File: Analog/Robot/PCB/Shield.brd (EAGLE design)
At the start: 160 x 100 mm, 5 parts, among them IC2 LM2574HVN-3.3

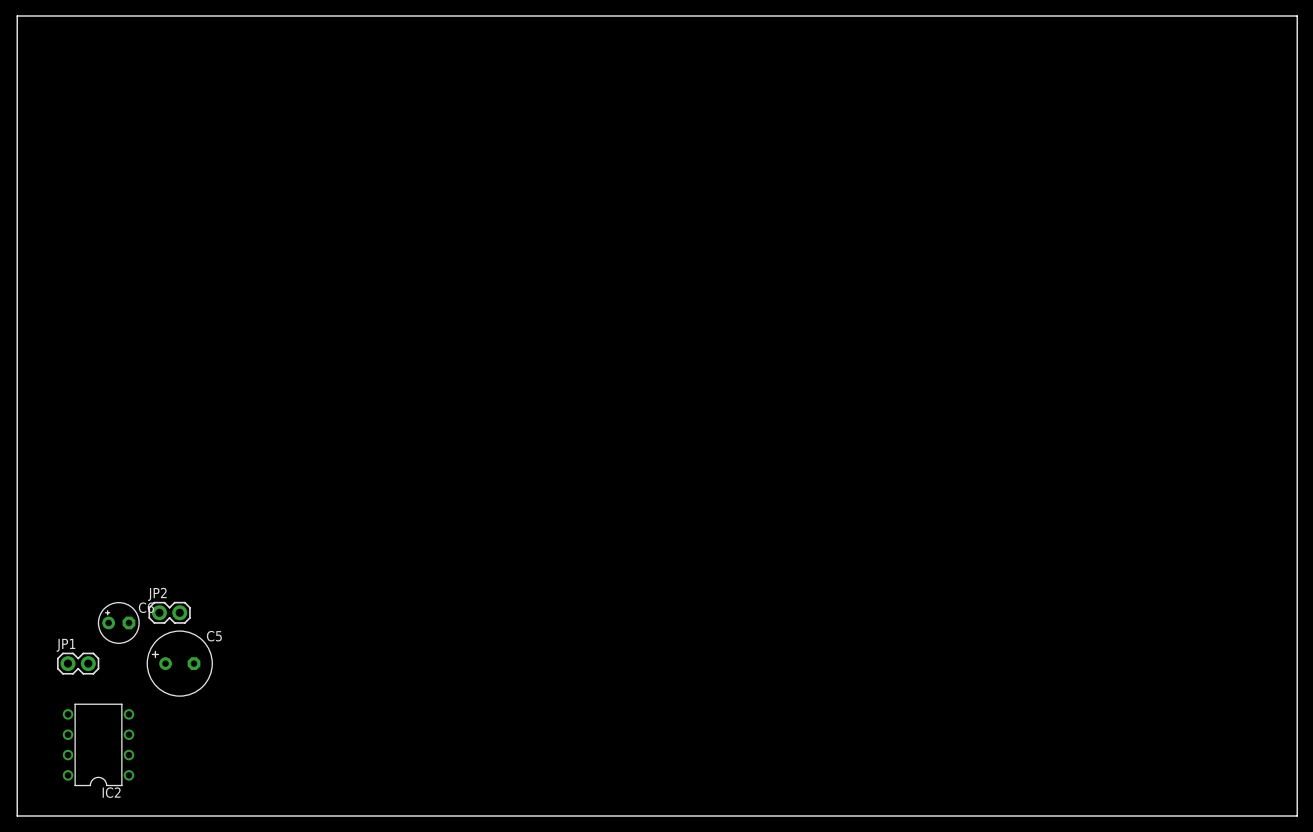
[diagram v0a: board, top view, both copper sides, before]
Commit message: PCB and firmware
Gate PCB 70% completed, need to figure out pinout for MCU and layout
signal amps.  Board size reduced by 50%.  Also need to add testpoints
Robot PCB PSU layout completed, motor and stepper drivers will move to
separate PCB
Created firmware files, w/o code
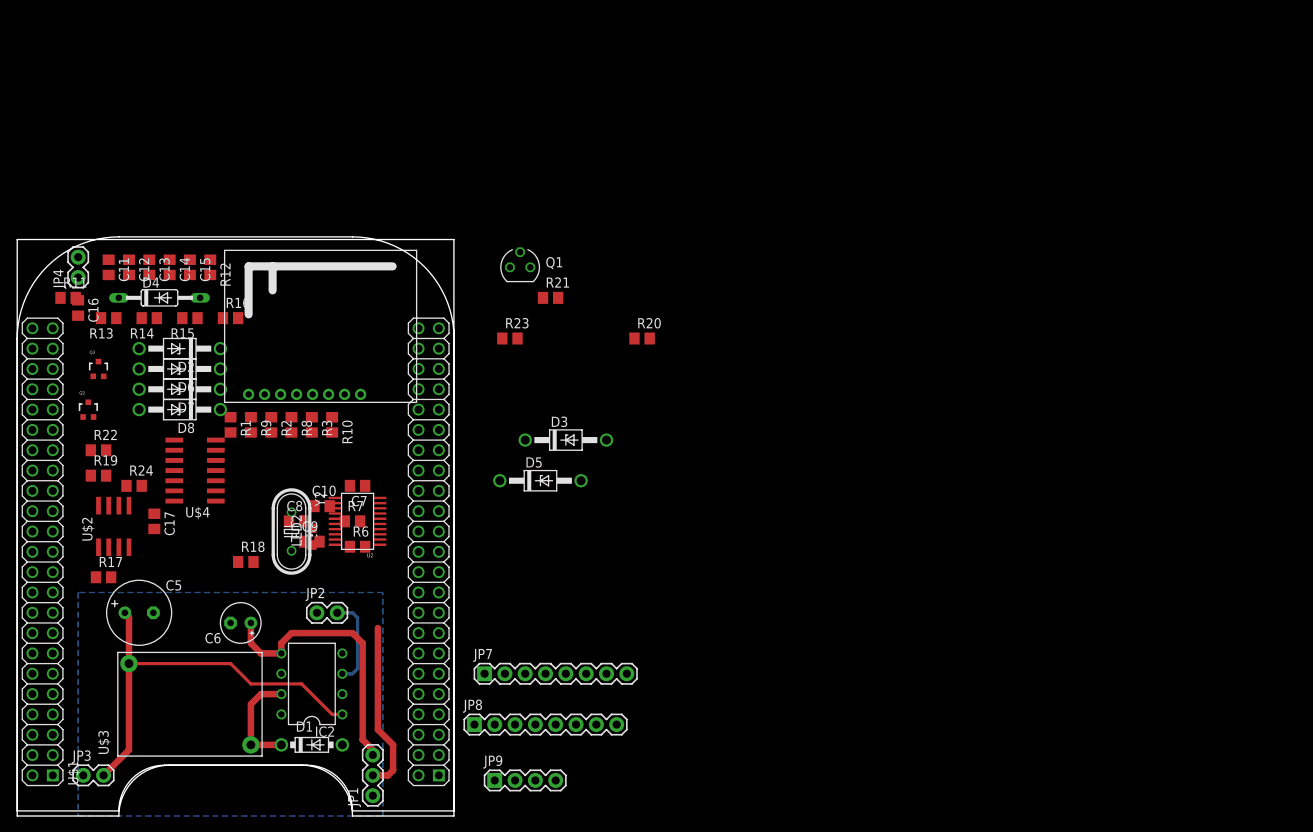
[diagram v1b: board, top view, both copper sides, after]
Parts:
- added C10: 1nF, rcl:C0805
- added C11, C12, C13, C14, C15, C16: (no value), rcl:C0805
- added C17: 10nF, rcl:C0805
- added C7: 0.1uF, rcl:C0805
- added C8, C9: 12pF, rcl:C0805
- added D1: 1N5819-B, diode:DO41-7.6
- added D2, D3, D7, D8: 1N4742A, diode:DO41Z10
- added D4: 1N4148DO35-10, diode:DO35-10
- added D5, D6: 1N4728, diode:DO41Z10
- added JP3, JP4: M02PTH, SparkFun-Connectors:1X02
- added JP7, JP8: (no value), SparkFun-Connectors:1X08
- added JP9: (no value), SparkFun-Connectors:1X04
- added LED2: (no value), led:CHIP-LED0805
- added Q1: BS250, transistor-small-signal:SOT54E
- added Q2, Q3: MOSFET-NCHANNEL2N7002PW, SparkFun-DiscreteSemi:SOT323
- added R1, R10, R12, R17, R18, R19, R2, R20, R21, R22, R23, R24, R3, R8, R9: 0, rcl:R0805
- added R11: 5k, rcl:R0805
- added R13, R14, R15, R16: 100k, rcl:R0805
- added R6: 47k, rcl:R0805
- added R7: 470, rcl:R0805
- added U$1: BEAGLEBONE_OUTLINE, adafruit:BEAGLEBONE_SHIELD
- added U$2: LM6482, npol:SOIC8
- added U$3: PE-526XXNL, npol:PE_VERTICAL
- added U$4: MAX4518, npol:SO-14
- added U2: MSP430G2X53_20P, npol:TSSOP20_PW
- added U3: QFM-TRX-24G, npol:QFM-TRX1-24G
- added Y2: (no value), SparkFun-FreqCtrl:HC49U-V
- JP1: value M02PTH -> (none); device SparkFun-Connectors:1X02 -> SparkFun-Connectors:1X03
- moved JP1 41.5 mm to (44.5, 2.54), turned to 90 degrees
- moved IC2 27.7 mm to (36.8, 16.5)
- moved JP2 19.7 mm to (37.5, 25.4)
- moved C6 15.2 mm to (27.9, 24.1), turned to 180 degrees
- moved C5 8.13 mm to (15.2, 25.4)
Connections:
- new net +12V: C17.1, C6.+, IC2.5, JP1.3, R21.2, R22.2, U$2.8, U$4.12
- new net AIN0: U$1.85
- new net DIR: JP7.1
- new net DLED: LED2.C, U2.2
- new net GNDA: C5.-, C6.-, D1.A, IC2.2, IC2.4, JP1.1, JP2.1, JP3.1
- new net MISO: U2.14
- new net MOSI: U2.15
- new net MUX_A0: U$4.1
- new net MUX_A1: U$4.14
- new net MUX_EN: U$4.2
- new net N$10: D4.A, Q1.G, R12.2
- new net N$11: C16.1, D2.C, D4.C, Q2.3, R13.2, U$4.4
- new net N$12: R20.1, R23.2, U$2.6
- new net N$13: R23.1, R24.2, U$2.7
- new net N$14: R18.2, U$4.6
- new net N$15: R17.2, R18.1, U$2.2
- new net N$16: R17.1, R19.2, U$2.1
- new net N$17: JP7.3, JP7.4
- new net N$18: D3.C, R13.1, R14.2, U$4.5
- new net N$19: D7.C, R14.1, R15.2, U$4.11
- new net N$2: LED2.A, R7.1
- new net N$20: D8.C, R15.1, R16.2, U$4.10
- new net N$21: Q1.S, R20.2, R21.1
- new net N$22: Q2.1, Q3.3, R22.1
- new net N$26: JP8.3, JP9.1
- new net N$27: JP8.4, JP9.2
- new net N$28: JP8.5, JP9.3
- new net N$29: JP8.6, JP9.4
- new net N$3: D1.C, IC2.7, U$3.2
- new net N$4: C5.+, IC2.1, JP3.2, U$3.1
- new net N$7: R2.1, R9.1, U3.3
- new net N$8: R1.1, R8.1, U3.2
- new net N$9: C11.1, C12.1, C13.1, C14.1, C15.1, JP4.2, R11.2, R12.1
- new net RFID_RX1: D6.C, R19.1, U2.9
- new net RFID_RX2: D5.C, R24.1, U2.10
- new net RFID_TX: Q3.1, U2.8
- new net RF_MISO: R10.2
- new net RF_MOSI: R8.2
- new net RF_SCK: R9.2
- new net RXD: U2.3
- new net SBWTCK: U2.17
- new net SBWTDIO: C10.1, R6.1, U2.16
- new net SCK: U2.7
- new net SPI0_CS: U$1.63
- new net SPI0_DI: R3.2, U$1.64
- new net SPI0_DO: R1.2, U$1.67
- new net SPI0_SCK: R2.2, U$1.68
- new net STEP: JP7.2
- new net SYS_5V: U$1.53
- new net TXD: U2.4
- new net V+: JP1.2, JP8.8
- new net VDD_5V: U$1.51, U$1.52
- new net XIN: C9.1, U2.19, Y2.2
- new net XOUT: C8.1, U2.18, Y2.1
- net +3V3: now also C7.1, JP8.2, R6.2, R7.2, U$1.49, U$1.50, U2.1, U3.1; no longer C5.+, IC2.1
- net GND: now also C10.2, C11.2, C12.2, C13.2, C14.2, C15.2, C16.2, C17.2, C7.2, C8.2, C9.2, D2.A, D3.A, D5.A, D6.A, D7.A, D8.A, JP4.1, JP8.1, JP8.7, Q1.D, Q2.2, Q3.2, R16.1, U$1.1, U$1.2, U$1.47, U$1.48, U$1.89, U$1.90, U$1.91, U$1.92, U$2.3, U$2.4, U$2.5, U$4.13, U$4.3, U2.20, U3.6; no longer C5.-, C6.-, IC2.2, IC2.4, JP1.1, JP2.1
- net N$5: now also R10.1, R3.1, U3.4; no longer C6.+, IC2.5, JP1.2
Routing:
- net N$4: track 0.00 -> 51.1 mm
- net +12V: track 0.00 -> 33.9 mm
- net V+: track 0.00 -> 21.4 mm
- net N$3: track 0.00 -> 13.2 mm
- net N$6: track 0.00 -> 11.3 mm
- added copper zone on layer 16, net GNDA
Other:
- board size 160 x 100 mm -> 54.6 x 72.1 mm

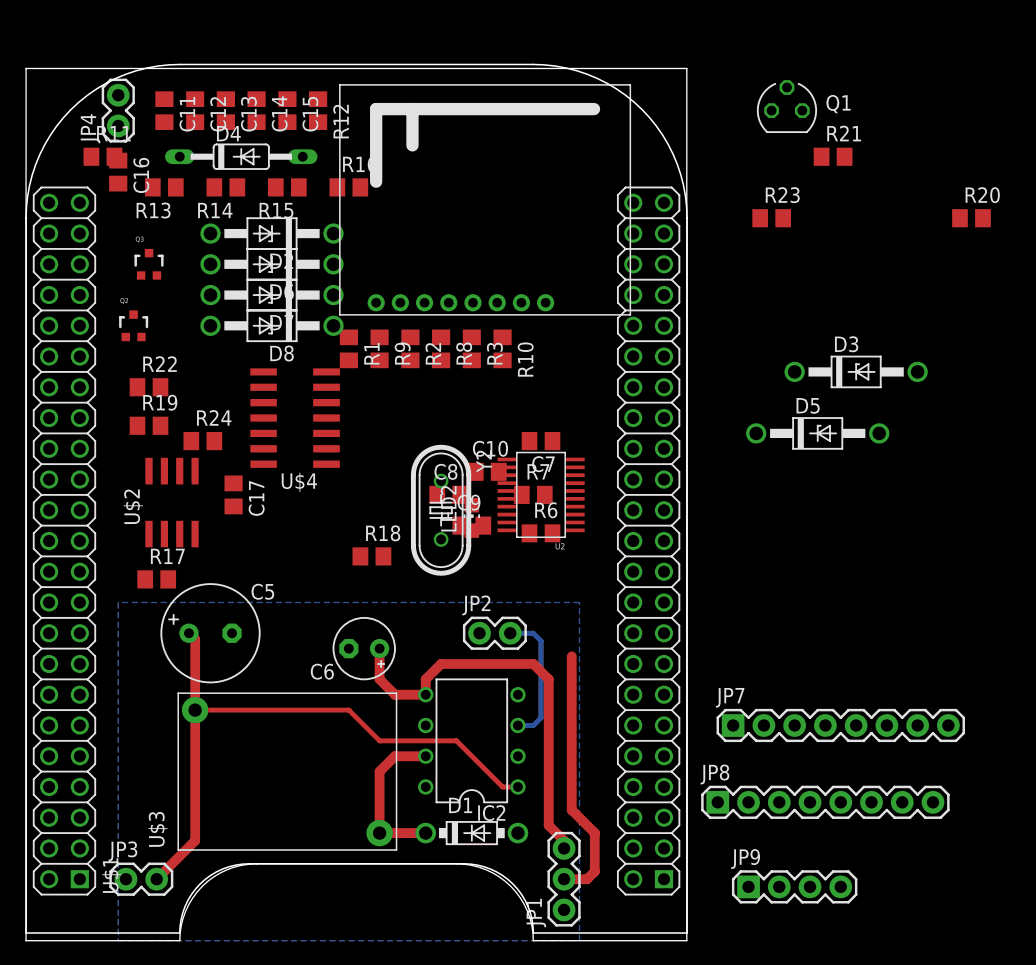
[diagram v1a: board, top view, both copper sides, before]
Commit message: Board final; SPI progress
Sent PCBs to FAB
SPI driver working for multi-byte.  Bug: bytes are sent in reversed
order, although bit ordering (MSB first) is correct.
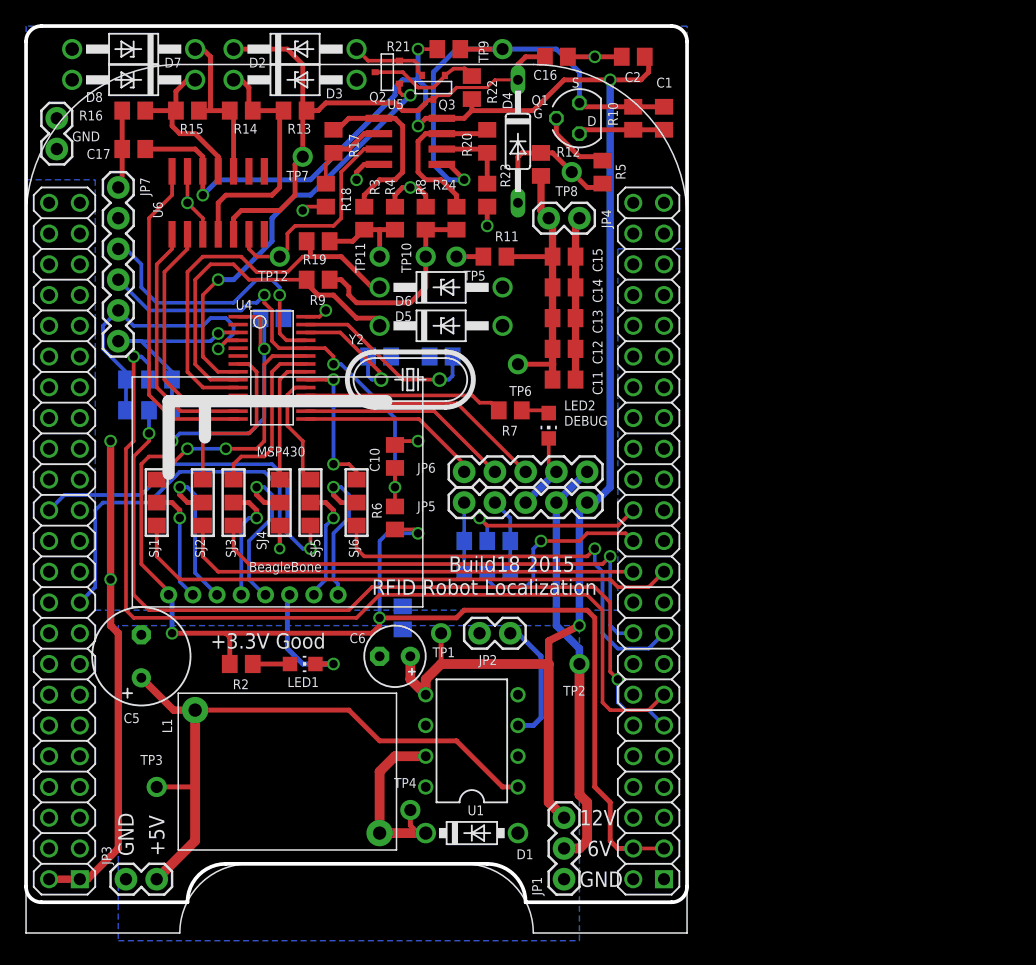
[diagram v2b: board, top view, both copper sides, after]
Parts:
- removed JP9: (no value), SparkFun-Connectors:1X04
- removed U$1: BEAGLEBONE_OUTLINE, adafruit:BEAGLEBONE_SHIELD
- removed U$2: LM6482, npol:SOIC8
- removed U$4: MAX4518, npol:SO-14
- added C1: 6.8n, rcl:C0805
- added C2: 100nF, rcl:C0805
- added JP5: MOTOR, SparkFun-Connectors:1X05
- added JP6: STEPPER, SparkFun-Connectors:1X05
- added LED1: (no value), led:CHIP-LED0805
- added R4: 10k, rcl:R0805
- added R5: 0, rcl:R0805
- added SJ1, SJ10, SJ2, SJ3, SJ4, SJ5, SJ6, SJ7, SJ8, SJ9: (no value), microbuilder:SOLDERJUMPER_2WAY_OPEN_0805
- added TP1, TP10, TP11, TP12, TP2, TP3, TP4, TP5, TP6, TP7, TP8, TP9: (no value), microbuilder:1X01_ROUND
- added U4: MSP430G2X53_28PPW, npol:PW(R-PDSO-G28)
- added U5: LM6482, npol:SOIC8
- added U6: MAX4518, npol:SO-14
- C16: value (none) -> 6.8n
- JP7: device SparkFun-Connectors:1X08 -> SparkFun-Connectors:1X06
- JP8: value (none) -> M02PTH; device SparkFun-Connectors:1X08 -> SparkFun-Connectors:1X02
- Q2, Q3: value MOSFET-NCHANNEL2N7002PW -> 2N7002_SINGLESOT23/TO-236AB; device SparkFun-DiscreteSemi:SOT323 -> npol:TO-236AB
- R10: value 0 -> 68k
- R13, R14, R15, R16: value 100k -> 12k
- R18, R23: value 0 -> DNP
- R2: value 0 -> 470
- R21: value 0 -> 100k
- R22, R24, R3, R8: value 0 -> 10k
- U2: value MSP430G2X53_20P -> BEAGLEBONE_OUTLINENODIMENSION; device npol:TSSOP20_PW -> npol:BEAGLEBONE_SHIELD_NODIMENSION
- moved JP8 76.8 mm to (2.54, 65.4), turned to 90 degrees
- moved JP7 67.5 mm to (7.62, 62.2), turned to 270 degrees
- moved U2 55.4 mm to (0.00, 1.27), turned to 0 degrees
- moved D3 52.3 mm to (22.2, 71.1)
- moved R20 40.5 mm to (38.1, 66.0), turned to 270 degrees
- moved C11 39.8 mm to (44.5, 46.4), turned to 0 degrees
- moved R17 39.0 mm to (25.4, 66.0), turned to 270 degrees
- moved JP4 38.9 mm to (45.7, 59.7), turned to 180 degrees
- moved C16 37.4 mm to (43.8, 73.0), turned to 0 degrees
- moved R22 36.4 mm to (36.8, 70.5), turned to 270 degrees
- moved C12 36.3 mm to (44.5, 48.9), turned to 0 degrees
- moved R11 33.4 mm to (38.7, 56.5)
- moved R21 33.0 mm to (34.9, 73.7), turned to 180 degrees
- moved C13 32.8 mm to (44.5, 51.4), turned to 0 degrees
- moved D5 32.4 mm to (34.3, 50.8)
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- renumbered IC2 to U1, U$3 to L1
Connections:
- removed net AIN0: U$1.85
- removed net N$26: JP8.3, JP9.1
- removed net N$28: JP8.5, JP9.3
- removed net N$29: JP8.6, JP9.4
- removed net N$5: R10.1, R3.1, U3.4
- removed net N$7: R2.1, R9.1, U3.3
- removed net RF_MISO: R10.2
- removed net RF_MOSI: R8.2
- removed net RF_SCK: R9.2
- removed net RXD: U2.3
- removed net SYS_5V: U$1.53
- removed net TXD: U2.4
- removed net VDD_5V: U$1.51, U$1.52
- new net BBB_G0: SJ5.3, U2.8.26
- new net BBB_G2: SJ4.3, U2.8.19
- new net CS: SJ6.1, U4.20
- new net ENABLE: JP6.1, U4.15
- new net GDO0: SJ5.1, U4.19
- new net GDO2: SJ4.1, U4.21
- new net M_RXD: JP5.1, SJ7.1, SJ8.3
- new net M_TXD: JP5.2, SJ7.3, SJ8.1
- new net N$1: R11.1, TP5.1
- new net N$23: Q1.G, R5.2
- new net P9_1-DGND: U2.9.1
- new net P9_2-DGND: U2.9.2
- new net P9_39-AIN0: U2.9.39
- new net P9_5-VDD_5V: U2.9.5
- new net P9_6-VDD_5V: U2.9.6
- new net P9_7-SYS_5V: U2.9.7
- new net RFCS: SJ6.2, U3.8
- new net RFGDO0: SJ5.2, U3.7
- new net RFGDO2: SJ4.2, U3.5
- new net RFSCLK: SJ2.2, U3.3
- new net RFSI: SJ1.2, U3.2
- new net RFSO: SJ3.2, U3.4
- new net RF_RXD: JP7.5, SJ10.3, SJ9.1, U4.4
- new net RF_TXD: JP7.6, SJ10.1, SJ9.3, U4.3
- new net RX1: SJ8.2, U2.9.26
- new net RX4: SJ10.2, U2.9.11
- new net TX1: SJ7.2, U2.9.24
- new net TX4: SJ9.2, U2.9.13
- new net VPROG: JP7.2
- net +12V: now also C2.1, JP5.5, TP1.1, U5.8, U6.12; no longer U$2.8, U$4.12
- net +3V3: now also R2.2, U2.9.3, U2.9.4, U4.1; no longer JP8.2, R7.2, U$1.49, U$1.50, U2.1
- net DIR: now also JP6.2, U4.16; no longer JP7.1
- net DLED: now also R7.2, U4.18; no longer LED2.C, U2.2
- net GND: now also C1.2, C2.2, JP5.3, JP6.4, JP7.1, JP8.2, LED1.C, LED2.C, R1.1, R10.1, R18.2, R23.2, R4.2, R8.2, U2.8.1, U2.8.2, U2.9.43, U2.9.44, U2.9.45, U2.9.46, U4.28, U5.4, U6.13, U6.3; no longer JP8.7, U$1.1, U$1.2, U$1.47, U$1.48, U$1.89, U$1.90, U$1.91, U$1.92, U$2.3, U$2.4, U$2.5, U$4.13, U$4.3, U2.20
- net GNDA: now also R1.2
- net MISO: now also SJ3.1, U4.22; no longer U2.14
- net MOSI: now also SJ1.1, U4.23; no longer U2.15
- net MUX_A0: now also U4.13, U6.1; no longer U$4.1
- net MUX_A1: now also U4.14, U6.14; no longer U$4.14
- net MUX_EN: now also U4.12, U6.2; no longer U$4.2
- net N$10: now also R5.1, TP8.1; no longer Q1.G
- net N$11: now also Q3.3, TP7.1, U6.5; no longer Q2.3, U$4.4
- net N$12: now also R20.2, R23.1, U5.6; no longer R20.1, R23.2, U$2.6
- net N$13: now also R20.1, U5.7; no longer R23.1, U$2.7
- net N$14: now also R17.2, R18.1, U5.2; no longer R18.2, U$4.6
- net N$15: now also R24.1, R8.1, R9.1, TP10.1; no longer R17.2, R18.1, U$2.2
- net N$16: now also R3.2, U5.1; no longer R19.2, U$2.1
- net N$17: now also R19.2, R3.1, R4.1, TP11.1; no longer JP7.3, JP7.4
- net N$18: now also U6.4; no longer U$4.5
- net N$19: now also U6.10; no longer U$4.11
- net N$20: now also U6.11; no longer U$4.10
- net N$21: now also C1.1, R10.2, TP9.1, U5.5; no longer R20.2
- net N$22: now also Q2.3, Q3.1; no longer Q2.1, Q3.3
- net N$27: now also LED1.A, R2.1; no longer JP8.4, JP9.2
- net N$3: now also TP4.1
- net N$4: now also TP3.1
- net N$8: now also TP12.1, U5.3, U6.6; no longer R1.1, R8.1, U3.2
- net N$9: now also TP6.1
- net RFID_RX1: now also D5.C, R9.2, U4.9; no longer D6.C, R19.1, U2.9
- net RFID_RX2: now also D6.C, R19.1, U4.10; no longer D5.C, R24.1, U2.10
- net RFID_TX: now also Q2.1, U4.8; no longer Q3.1, U2.8
- net SBWTCK: now also JP7.3, U4.25; no longer U2.17
- net SBWTDIO: now also JP7.4, U4.24; no longer U2.16
- net SCK: now also SJ2.1, U4.7; no longer U2.7
- net SPI0_CS: now also SJ6.3, U2.9.17; no longer U$1.63
- net SPI0_DI: now also SJ3.3, U2.9.18; no longer R3.2, U$1.64
- net SPI0_DO: now also SJ1.3, U2.9.21; no longer R1.2, U$1.67
- net SPI0_SCK: now also SJ2.3, U2.9.22; no longer R2.2, U$1.68
- net STEP: now also JP6.3, U4.17; no longer JP7.2
- net V+: now also JP5.4, JP6.5, TP2.1; no longer JP8.8
- net XIN: now also U4.27; no longer U2.19
- net XOUT: now also U4.26; no longer U2.18
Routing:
- net GND: track 0.00 -> 117.1 mm, vias 0 -> 11
- net +3V3: track 0.00 -> 114.6 mm, vias 0 -> 5
- net +12V: track 33.9 -> 144.7 mm, vias 0 -> 5
- net TX4: track 0.00 -> 78.5 mm, vias 0 -> 1
- net RX4: track 0.00 -> 70.1 mm, vias 0 -> 2
- net N$11: track 0.00 -> 47.6 mm
- net SPI0_DO: track 0.00 -> 46.0 mm
- net SPI0_DI: track 0.00 -> 41.7 mm, vias 0 -> 1
- net N$21: track 0.00 -> 39.9 mm, vias 0 -> 1
- net SBWTDIO: track 0.00 -> 39.8 mm, vias 0 -> 3
- net SPI0_SCK: track 0.00 -> 38.6 mm
- net SPI0_CS: track 0.00 -> 35.5 mm, vias 0 -> 1
- net RFID_TX: track 0.00 -> 35.3 mm, vias 0 -> 2
- net RFID_RX2: track 0.00 -> 33.3 mm
- net BBB_G2: track 0.00 -> 32.2 mm, vias 0 -> 1
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- added copper zone on layer 16, net GND
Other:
- board size 54.6 x 72.1 mm -> 54.6 x 72.4 mm
- board text added: "+3.3V Good"
- board text added: "+5V"
- board text added: "12V"
- board text added: "2014 Nishant Pol"
- board text added: "6V"
- board text added: "BeagleBone"
- board text added: "Build18 2015"
- board text added: "D"
- board text added: "DEBUG"
- board text added: "G"
- board text added: "GND"
- board text added: "MSP430"
- board text added: "RFID Robot Localization"
- board text added: "S"
